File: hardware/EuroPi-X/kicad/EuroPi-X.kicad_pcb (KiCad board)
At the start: 2 copper layers, 102.9 x 109.2 mm, 167 parts, among them J1 Conn_01x16_Pin, J10 Thonkiconn_Mono_Jack, J11 Conn_02x08_Odd_Even, J12 Thonkiconn_Mono_Jack, J13 Thonkiconn_Mono_Jack, J14 Thonkiconn_Mono_Jack, J15 Thonkiconn_Mono_Jack, J16 Thonkiconn_Mono_Jack, J17 Thonkiconn_Mono_Jack, J18 Conn_01x03_Pin, J2 Conn_01x16_Pin, J22 Conn_01x11_Pin, J3 Thonkiconn_Mono_Jack, J4 Thonkiconn_Mono_Jack, J5 Conn_01x16_Pin, J6 Thonkiconn_Mono_Jack, J7 Thonkiconn_Mono_Jack, J8 Conn_01x16_Pin, J9 Thonkiconn_Mono_Jack, P1 USB_C_Plug_USB2.0, P2 Potentiometer_9mm_Vertical_Li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, P3 Potentiometer_9mm_Vertical_Li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, Q1 BSS138, SW1 B1, SW2 B2, U1 MCP6002-xSN, U10 MCP3428, U11 L7805, U12 LM4040DBZ-4.1, U2 LM4040DBZ-2.0, U3 LM4040DBZ-10, U4 RP2040, U7 TL074, U8 TL074, U9 MCP6004, Y1 Crystal_GND2

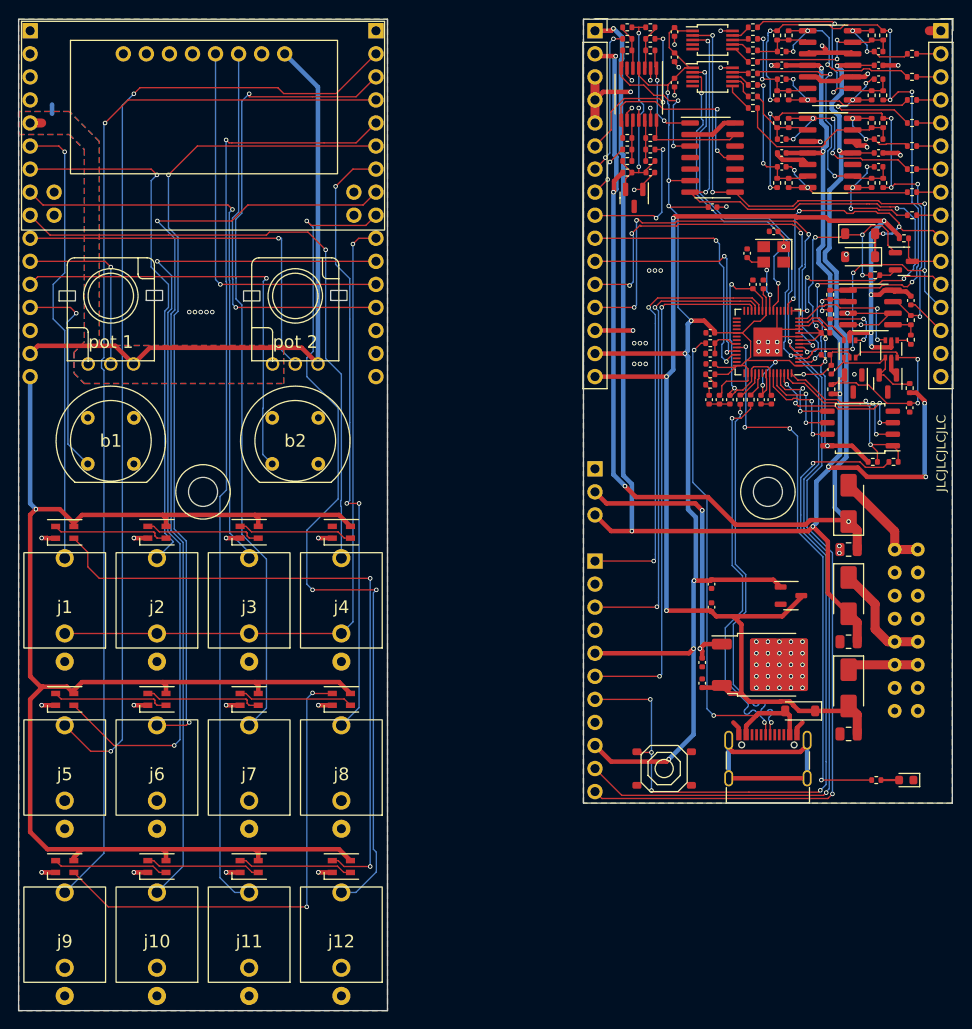
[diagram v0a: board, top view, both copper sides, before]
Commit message: added mouse bites and combined the pcbs in kicad to allow producing them together used the mouse bites from miniOSC from benjiaomodular
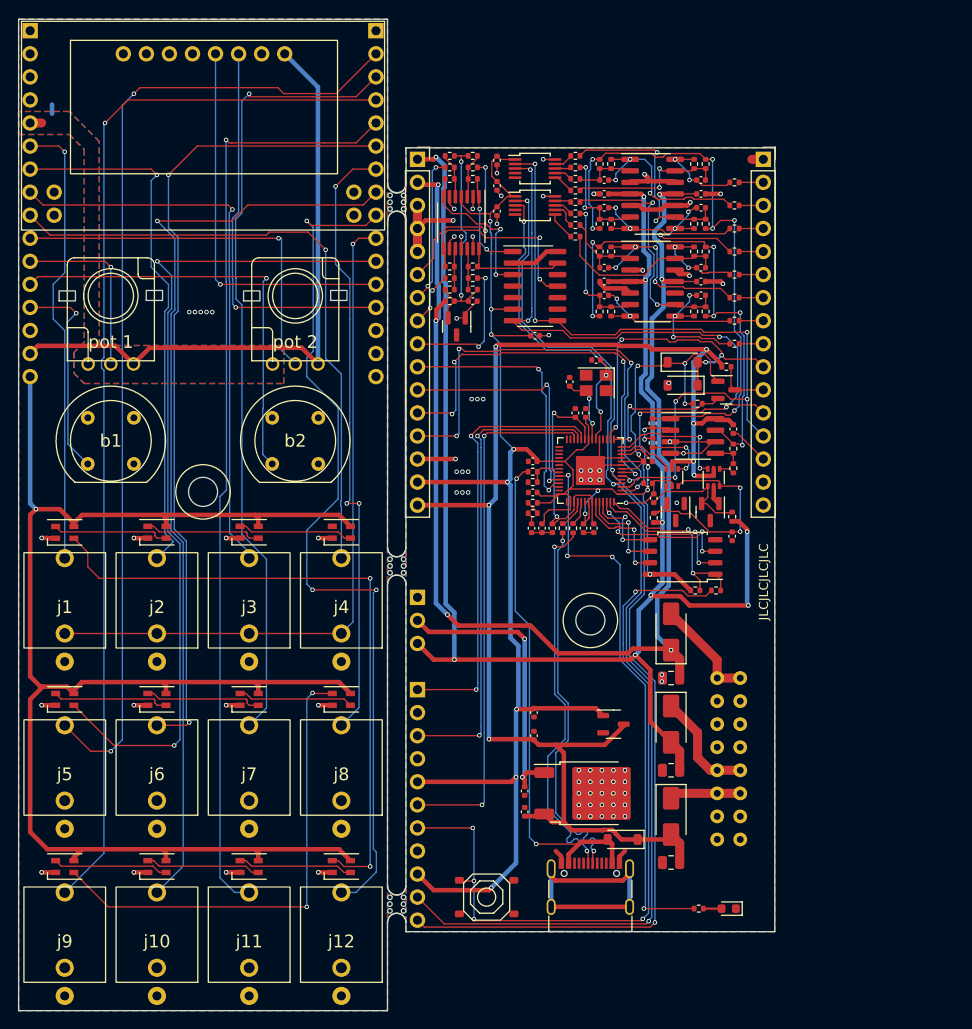
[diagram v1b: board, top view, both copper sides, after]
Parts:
- added mouse-bite-2mm-slot: VAL**, Panelization:mouse-bite-2mm-slot, F.Cu at (41.7, 60.2)
- added mouse-bite-2mm-slot: VAL**, Panelization:mouse-bite-2mm-slot, F.Cu at (41.7, 97.5)
- added mouse-bite-2mm-slot: VAL**, Panelization:mouse-bite-2mm-slot, F.Cu at (41.7, 20.2)
- moved G*** 24.9 mm to (62.4, 46.4)
- moved C35 24.1 mm to (55.8, 85.0)
- moved C39 24.1 mm to (69.3, 48.7)
- moved D7 24.1 mm to (78.2, 98.0)
- moved R55 24.1 mm to (78.7, 49.5)
- moved SW3 24.1 mm to (51.6, 96.7)
- moved U5 24.1 mm to (65.5, 77.7)
- moved C11 24.1 mm to (75.2, 17.7)
- moved C12 24.1 mm to (75.2, 27.4)
- moved C14 24.1 mm to (69.3, 51.1)
- moved C16 24.1 mm to (63.4, 56.1)
- moved C18 24.1 mm to (78.7, 45.1)
- moved C2 24.1 mm to (78.6, 57.0)
- moved C22 24.1 mm to (75.2, 28.9)
- moved C24 24.1 mm to (75.2, 19.2)
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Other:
- board size 102.9 x 109.2 mm -> 83.3 x 109.2 mm
